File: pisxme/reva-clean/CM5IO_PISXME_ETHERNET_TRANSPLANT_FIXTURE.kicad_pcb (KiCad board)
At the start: 6 copper layers, 6 parts, among them J2 A70-112-331N126, J7 Raspberry-Pi-5-Compute-Module, J9 THD-02-R, U6 TPD4EUSB30, U9 TPD4EUSB30

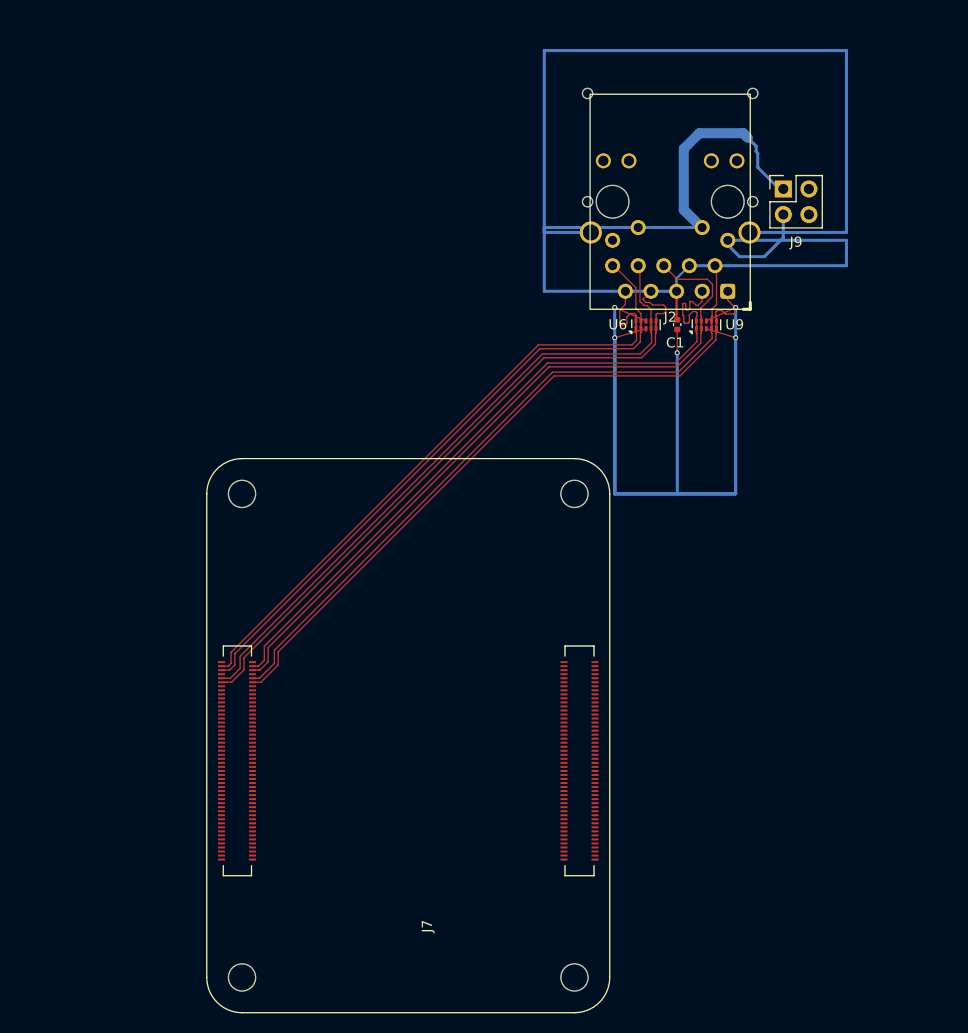
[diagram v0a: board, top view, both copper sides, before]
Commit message: phase17: record support adaptation experiment
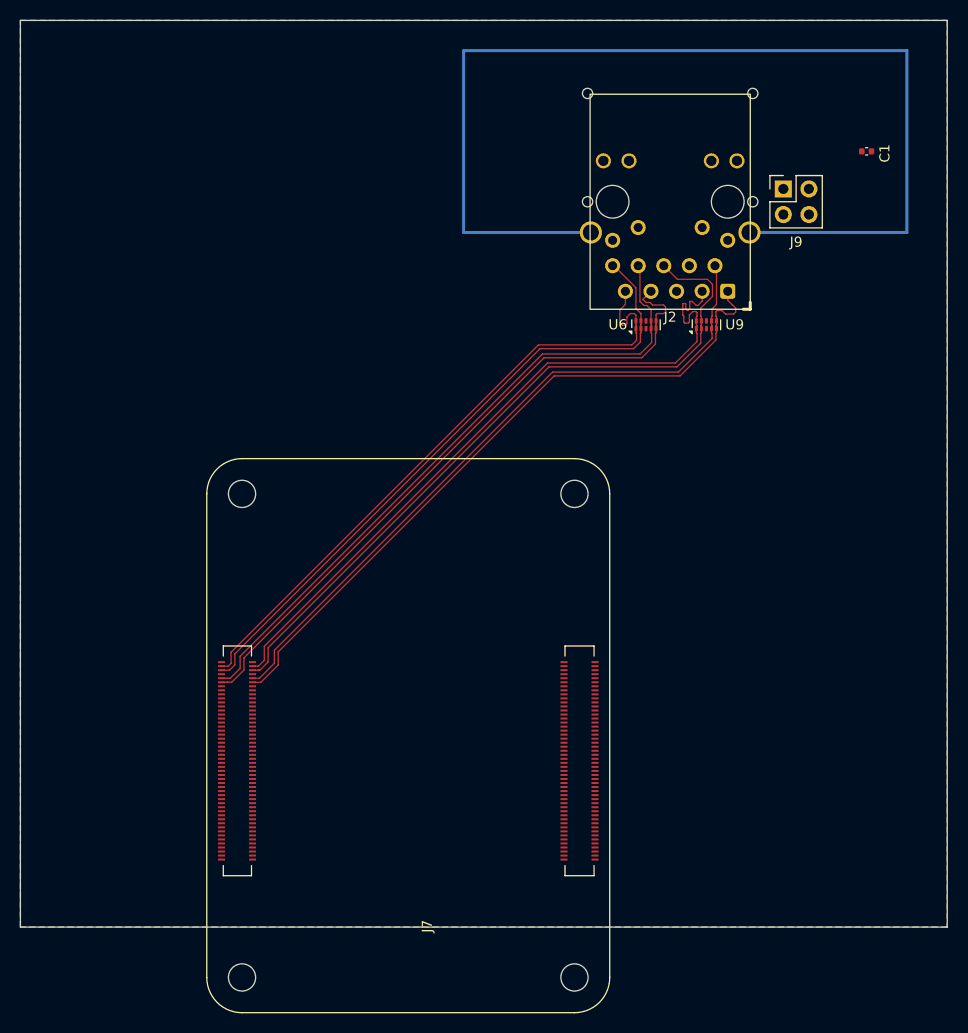
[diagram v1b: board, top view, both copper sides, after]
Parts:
- moved C1 25.5 mm to (92.0, 48.0), turned to 0 degrees
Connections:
- J2 pad 11: ETH_CT1 -> ETH_CT_COMMON
- J2 pad 12: ETH_CT2 -> ETH_CT_COMMON
- J2 pad 13: ETH_CT3 -> ETH_CT_COMMON
- J2 pad 14: ETH_CT4 -> ETH_CT_COMMON
- J9 pad 1: ETH_CT2 -> ETH_CT_COMMON
- J9 pad 2: ETH_CT3 -> ETH_CT_COMMON
- J9 pad 3: ETH_CT1 -> ETH_CT_COMMON
- J9 pad 4: ETH_CT4 -> ETH_CT_COMMON
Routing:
- net ETH_GND: track 121.1 -> 0.00 mm, vias 5 -> 0
- net ETH_CT3: track 72.4 -> 0.00 mm
- net ETH_CT2: track 57.4 -> 0.00 mm
- net ETH_CT1: track 39.3 -> 0.00 mm
- net ETH_CT4: track 38.3 -> 0.00 mm
- net GBE_SHIELD: track 80.3 -> 108.3 mm
- net ETH_CT_COMMON: track 5.83 -> 0.00 mm
- added copper zone on In2.Cu, net ETH_CT_COMMON
- added copper zone on B.Cu, net ETH_GND
- added copper zone on F.Cu, net ETH_GND
- added copper zone on In1.Cu, net ETH_GND
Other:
- board outline added: 92 x 90 mm

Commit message: phase17: publish explicit support fanout blocker
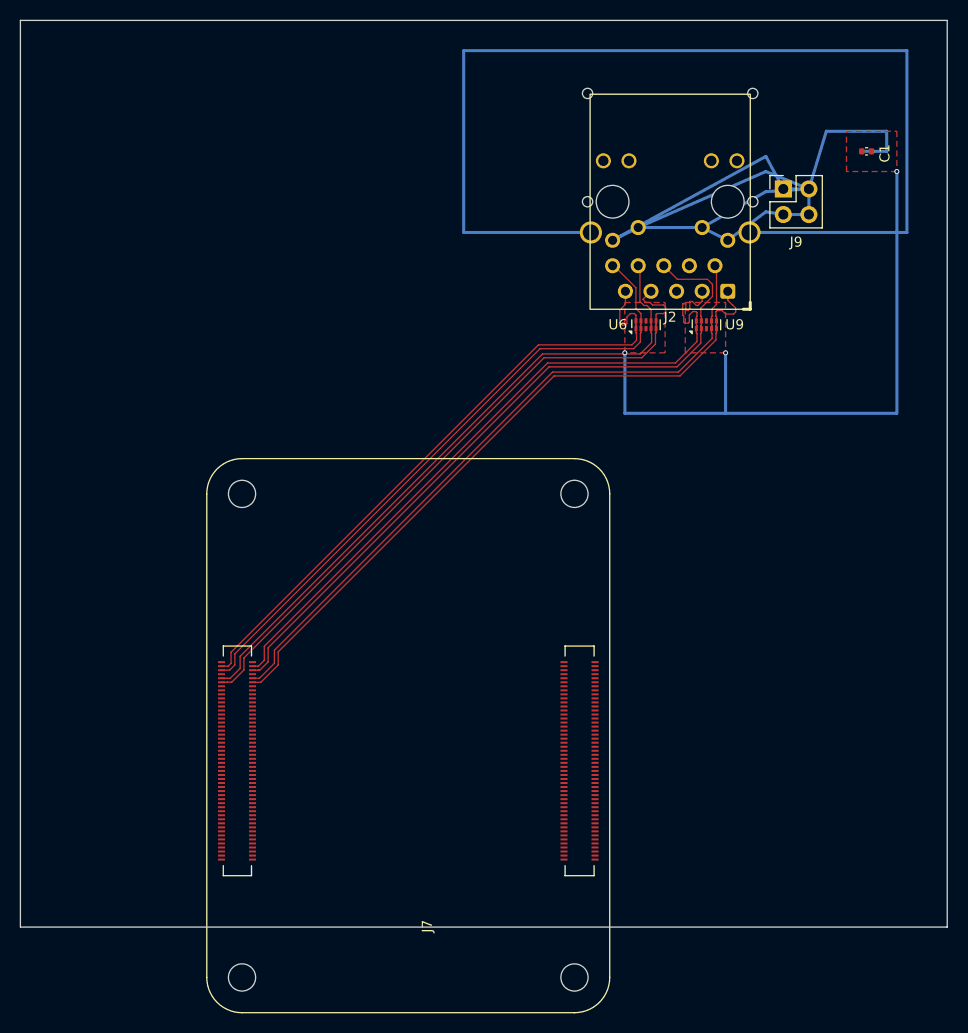
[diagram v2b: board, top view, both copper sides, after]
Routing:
- net ETH_CT_COMMON: track 0.00 -> 93.6 mm
- net ETH_GND: track 0.00 -> 63.0 mm, vias 0 -> 3
- removed copper zone on In2.Cu, net ETH_CT_COMMON
- removed copper zone on B.Cu, net ETH_GND

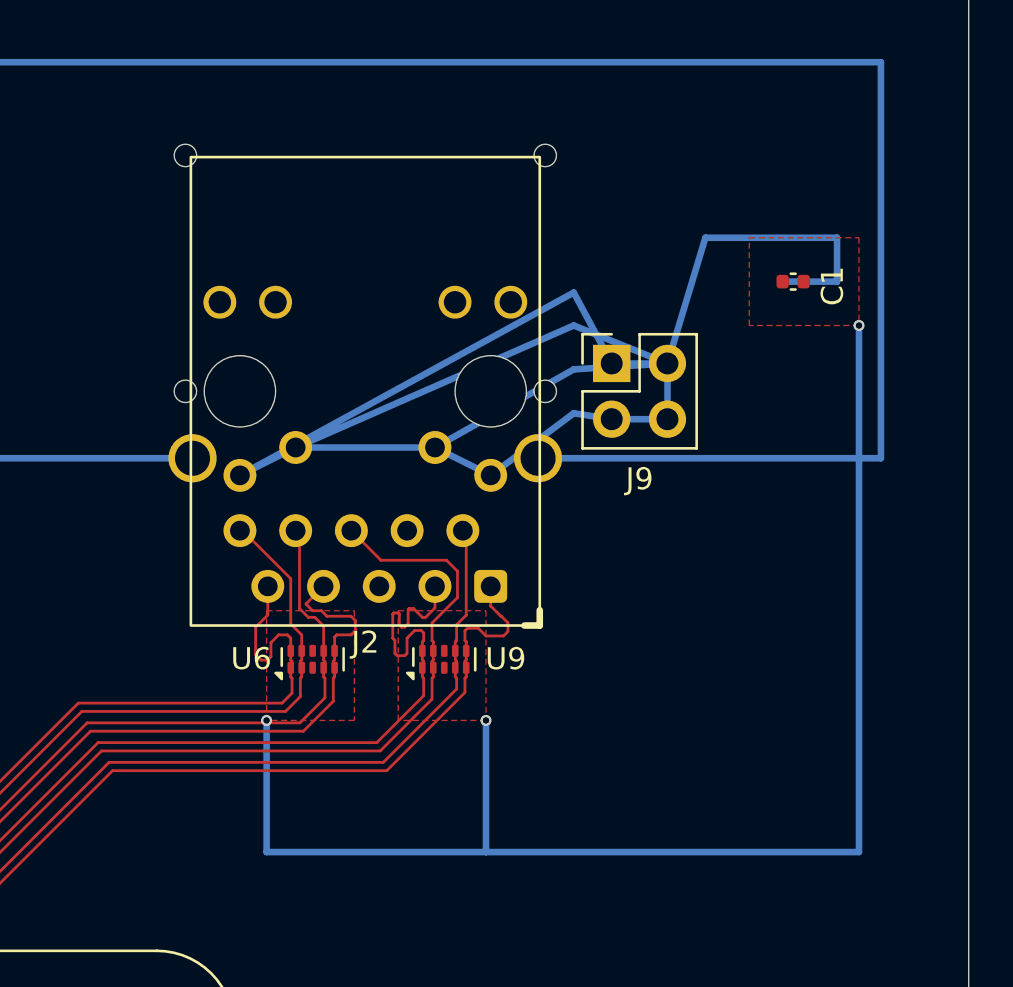
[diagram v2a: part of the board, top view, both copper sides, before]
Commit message: phase17: close CM5IO disposable fixture gate
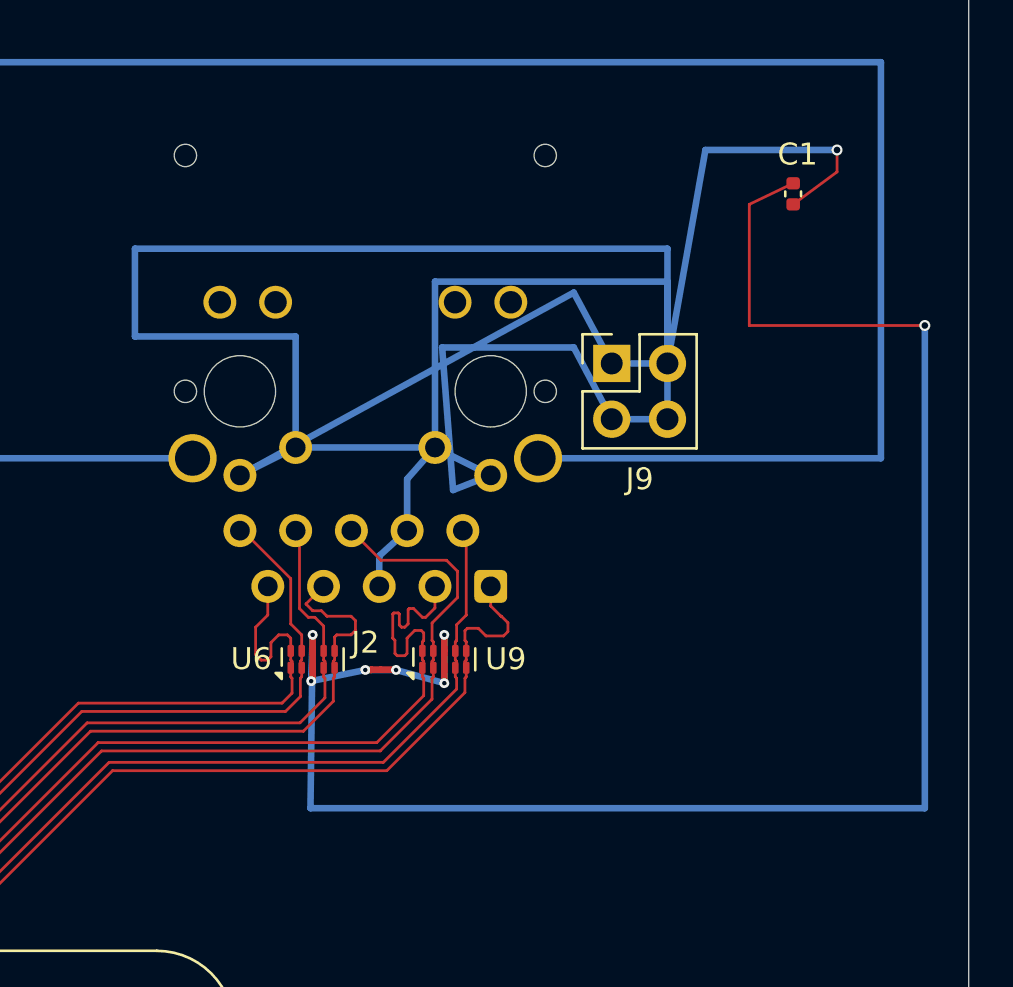
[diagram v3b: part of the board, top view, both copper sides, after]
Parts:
- moved C1 4.00 mm to (92.0, 44.0), turned to 90 degrees
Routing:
- net ETH_CT_COMMON: track 93.6 -> 153.2 mm, vias 0 -> 1
- net ETH_GND: track 63.0 -> 89.9 mm, vias 3 -> 7
- removed copper zone on F.Cu, net ETH_GND
- removed copper zone on In1.Cu, net ETH_GND

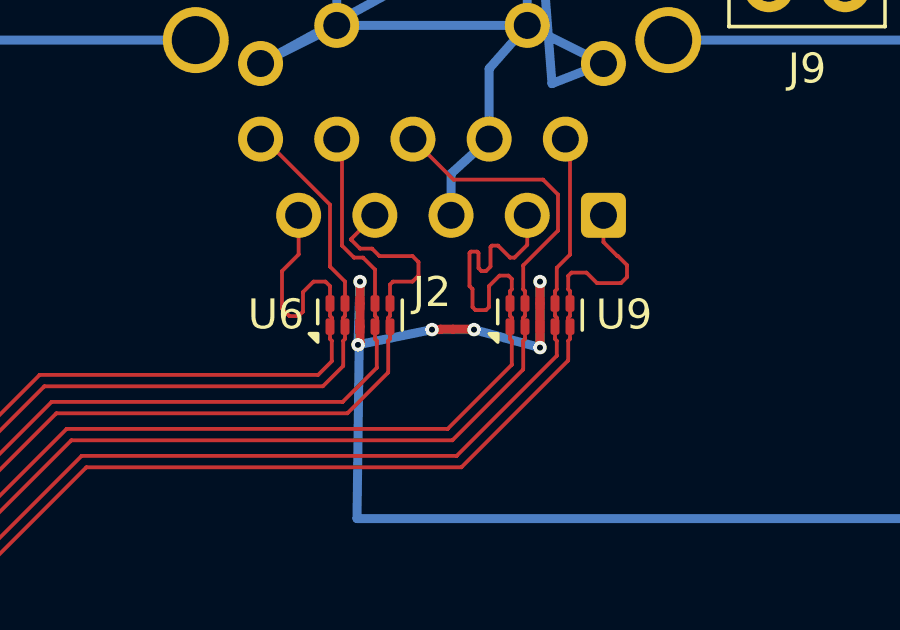
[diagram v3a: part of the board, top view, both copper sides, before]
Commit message: phase17: align Ethernet with CM5IO EDAC geometry
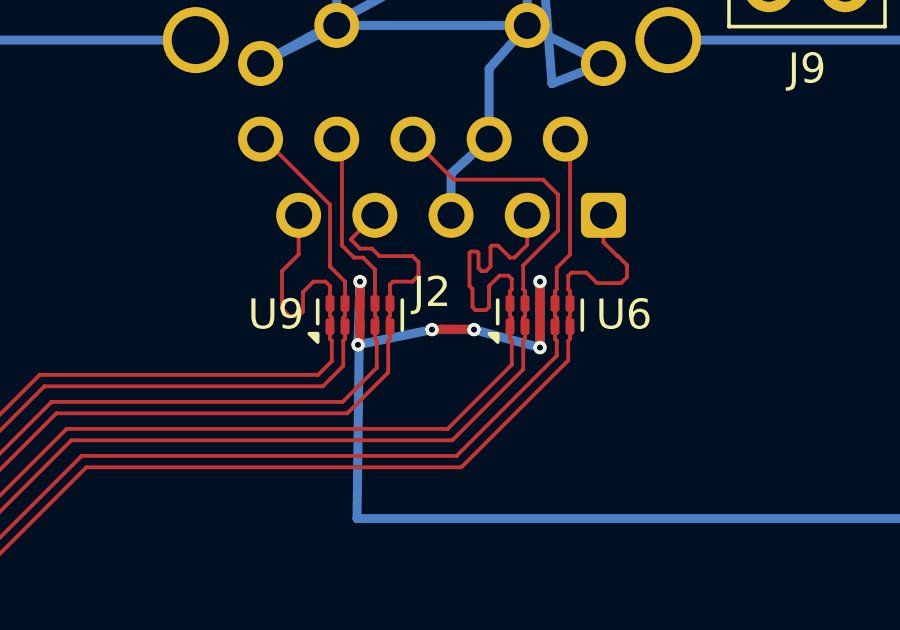
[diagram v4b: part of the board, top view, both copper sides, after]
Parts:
- renumbered U9 to U6, U6 to U9

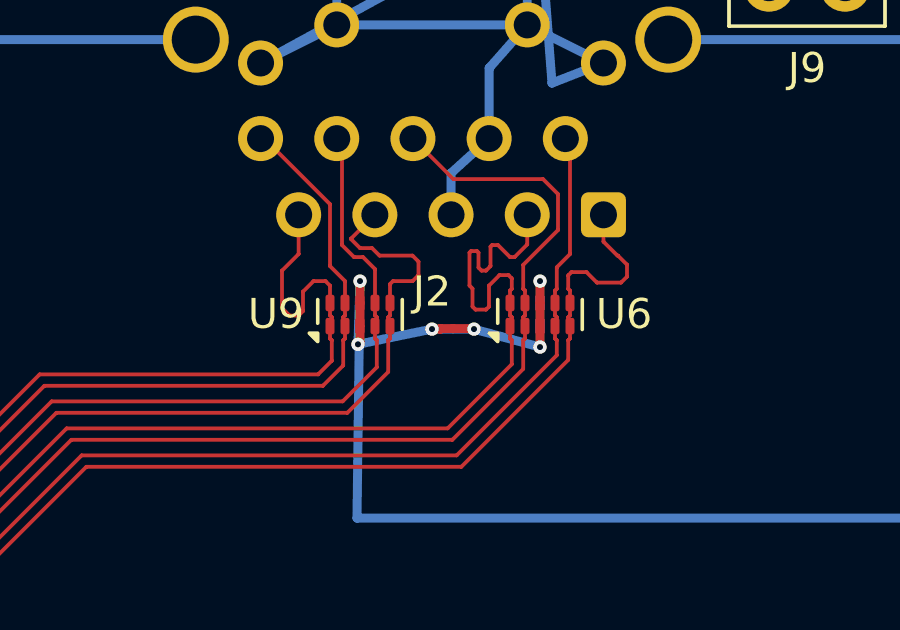
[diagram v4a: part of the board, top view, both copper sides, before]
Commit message: phase17: correct CM5IO Ethernet transplant authority
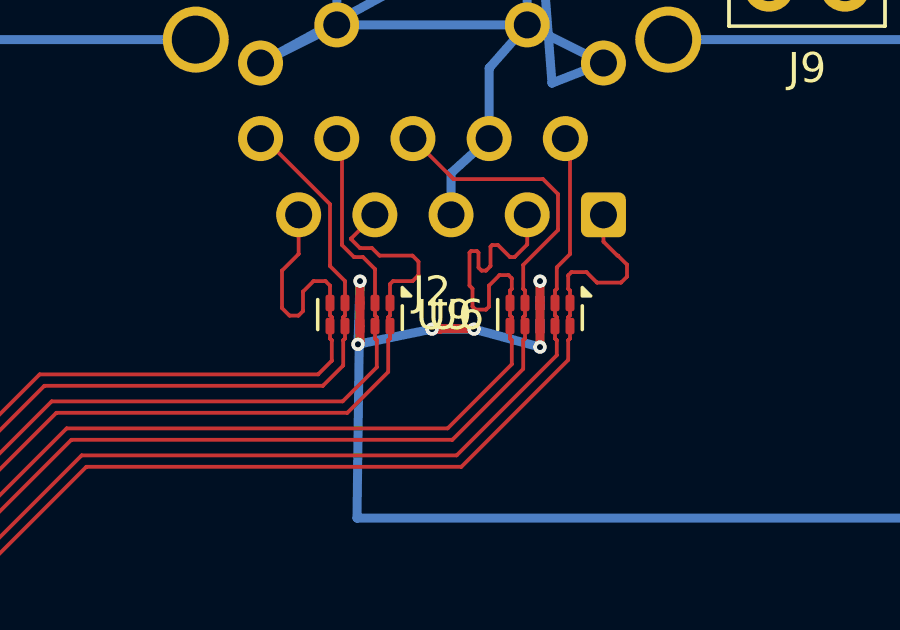
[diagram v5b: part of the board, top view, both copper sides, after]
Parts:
- turned U6 to -90 degrees
- turned U9 to -90 degrees
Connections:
- U6 pad 1: CM5_GBE_TD1_P -> CM5_GBE_TD0_P
- U6 pad 10: CM5_GBE_TD1_P -> CM5_GBE_TD0_P
- U6 pad 2: CM5_GBE_TD1_N -> CM5_GBE_TD0_N
- U6 pad 4: CM5_GBE_TD0_N -> CM5_GBE_TD1_N
- U6 pad 5: CM5_GBE_TD0_P -> CM5_GBE_TD1_P
- U6 pad 6: CM5_GBE_TD0_P -> CM5_GBE_TD1_P
- U6 pad 7: CM5_GBE_TD0_N -> CM5_GBE_TD1_N
- U6 pad 9: CM5_GBE_TD1_N -> CM5_GBE_TD0_N
- U9 pad 1: CM5_GBE_TD3_P -> CM5_GBE_TD2_P
- U9 pad 10: CM5_GBE_TD3_P -> CM5_GBE_TD2_P
- U9 pad 2: CM5_GBE_TD3_N -> CM5_GBE_TD2_N
- U9 pad 4: CM5_GBE_TD2_N -> CM5_GBE_TD3_N
- U9 pad 5: CM5_GBE_TD2_P -> CM5_GBE_TD3_P
- U9 pad 6: CM5_GBE_TD2_P -> CM5_GBE_TD3_P
- U9 pad 7: CM5_GBE_TD2_N -> CM5_GBE_TD3_N
- U9 pad 9: CM5_GBE_TD3_N -> CM5_GBE_TD2_N
